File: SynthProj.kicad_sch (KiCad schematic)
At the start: 36 parts, among them J18 Ext In, SW5 SW_DPDT_x2

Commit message: more and more routing
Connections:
- net VCA/Main_Out: now also SW5.3 (C)
- net EchoOut: now reaches SW5.6 (C)
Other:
- note added: "Switch in the echo effect or use the jacks"
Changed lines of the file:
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@@
 (kicad_sch (version 20230121) (generator eeschema)
   (paper "A3")
+  (junction (at 224.155 65.405) (diameter 0) (color 0 0 0 0)
+  )
+  (junction (at 254.635 162.56) (diameter 0) (color 0 0 0 0)
+  )
   (junction (at 181.61 97.155) (diameter 0) (color 0 0 0 0)
   )
   (junction (at 74.93 88.265) (diameter 0) (color 0 0 0 0)
   )
-  (junction (at 224.155 67.945) (diameter 0) (color 0 0 0 0)
-  )
   (junction (at 134.62 162.56) (diameter 0) (color 0 0 0 0)
   )
@@
     (stroke (width 0) (type default))
   )
+  (wire (pts (xy 254.635 108.585) (xy 280.035 108.585))
+    (stroke (width 0) (type default))
+  )
   (wire (pts (xy 72.39 62.865) (xy 81.28 62.865))
     (stroke (width 0) (type default))
@@
     (stroke (width 0) (type default))
   )
-  (wire (pts (xy 351.79 80.01) (xy 363.855 80.01))
+  (wire (pts (xy 217.17 67.945) (xy 243.84 67.945))
+    (stroke (width 0) (type default))
+  )
+  (wire (pts (xy 351.79 80.01) (xy 356.87 80.01))
     (stroke (width 0) (type default))
   )
@@
     (stroke (width 0) (type default))
   )
-  (wire (pts (xy 217.17 67.945) (xy 224.155 67.945))
-    (stroke (width 0) (type default))
-  )
   (wire (pts (xy 175.26 97.155) (xy 181.61 97.155))
     (stroke (width 0) (type default))
@@
     (stroke (width 0) (type default))
   )
-  (wire (pts (xy 217.17 65.405) (xy 229.87 65.405))
+  (wire (pts (xy 217.17 65.405) (xy 224.155 65.405))
     (stroke (width 0) (type default))
   )
@@
     (stroke (width 0) (type default))
   )
+  (wire (pts (xy 254.635 162.56) (xy 266.7 162.56))
+    (stroke (width 0) (type default))
+  )
   (wire (pts (xy 181.61 97.155) (xy 186.69 97.155))
     (stroke (width 0) (type default))
@@
     (stroke (width 0) (type default))
   )
-  (wire (pts (xy 245.11 162.56) (xy 266.7 162.56))
+  (wire (pts (xy 245.11 162.56) (xy 254.635 162.56))
     (stroke (width 0) (type default))
   )
@@
     (stroke (width 0) (type default))
   )
+  (wire (pts (xy 224.155 65.405) (xy 229.87 65.405))
+    (stroke (width 0) (type default))
+  )
   (wire (pts (xy 74.93 57.785) (xy 81.28 57.785))
     (stroke (width 0) (type default))
@@
     (stroke (width 0) (type default))
   )
+  (wire (pts (xy 254.635 162.56) (xy 254.635 108.585))
+    (stroke (width 0) (type default))
+  )
   (wire (pts (xy 132.08 118.745) (xy 132.08 79.375))
     (stroke (width 0) (type default))
@@
     (stroke (width 0) (type default))
   )
+  (wire (pts (xy 133.985 96.52) (xy 144.78 96.52))
+    (stroke (width 0) (type default))
+  )
   (wire (pts (xy 78.74 133.985) (xy 81.28 133.985))
     (stroke (width 0) (type default))
@@
     (stroke (width 0) (type default))
   )
-  (wire (pts (xy 269.24 108.585) (xy 280.035 108.585))
-    (stroke (width 0) (type default))
-  )
   (wire (pts (xy 105.41 116.205) (xy 129.54 116.205))
     (stroke (width 0) (type default))
@@
     (stroke (width 0) (type default))
   )
-  (wire (pts (xy 224.155 67.945) (xy 224.155 92.71))
+  (wire (pts (xy 133.985 84.455) (xy 133.985 96.52))
     (stroke (width 0) (type default))
   )
@@
     (stroke (width 0) (type default))
   )
-  (wire (pts (xy 224.155 67.945) (xy 243.84 67.945))
-    (stroke (width 0) (type default))
-  )
   (wire (pts (xy 241.935 120.65) (xy 235.585 120.65))
     (stroke (width 0) (type default))
@@
     (stroke (width 0) (type default))
   )
+  (wire (pts (xy 224.155 65.405) (xy 224.155 92.71))
+    (stroke (width 0) (type default))
+  )
   (wire (pts (xy 372.745 158.115) (xy 368.935 158.115))
     (stroke (width 0) (type default))
@@
   )
   (wire (pts (xy 338.455 82.55) (xy 341.63 82.55))
+    (stroke (width 0) (type default))
+  )
+  (wire (pts (xy 136.525 84.455) (xy 133.985 84.455))
     (stroke (width 0) (type default))
   )
@@
     (effects (font (size 1.27 1.27)) (justify left bottom))
   )
+  (text "Switch in the echo effect or use the jacks" (at 319.405 71.755 0)
+    (effects (font (size 1.27 1.27)) (justify left bottom))
+  )
   (text "100k 20mm Linear Pot: RK09D1130-F20-C0-B104\n100k 20mm Log Pot: RK09D1130-F20-C0-A104\n\n10k 20mm Linear Pot: RK09D1130-F20-C0-B103\n10k 20mm Log Pot: RK09D1130-F20-C0-V103"
     (at 23.495 234.315 0)
@@
   (text "12 Pole Rotary Switch - Metal MC12L1NCQD 9.4mm shoulder height\n12 Pole Rotary Switch - Plastic RTAP31S12W25FS 12.6mm shoulder height\n12 Pole Rotary Switch - Plastic KC52A10.001NPS 14.2mm shoulder height\n12 Pole Rotary Switch - Plastic SR2612F-0112-21R0B-D8-N 12.6mm shoulder height "
     (at 23.495 263.525 0)
+    (effects (font (size 1.27 1.27)) (justify left bottom))
+  )
+  (label "EchoOut" (at 144.78 96.52 0) (fields_autoplaced)
+    (effects (font (size 1.27 1.27)) (justify left bottom))
+  )
+  (label "EchoOut" (at 356.87 80.01 0) (fields_autoplaced)
     (effects (font (size 1.27 1.27)) (justify left bottom))
   )
@@
     )
   )
+  (global_label "AD1A" (shape input) (at 236.855 67.945 270) (fields_autoplaced)
+    (effects (font (size 1.27 1.27)) (justify right))
+    (property "Intersheetrefs" "${INTERSHEET_REFS}" (at 236.855 74.9327 90)
+      (effects (font (size 1.27 1.27)) (justify right) hide)
+    )
+  )
   (global_label "S&H" (shape input) (at 68.58 123.825 180) (fields_autoplaced)
     (effects (font (size 1.27 1.27)) (justify right))
@@
     )
   )
-  (global_label "AD1A" (shape input) (at 201.295 92.71 90) (fields_autoplaced)
-    (effects (font (size 1.27 1.27)) (justify left))
-    (property "Intersheetrefs" "${INTERSHEET_REFS}" (at 201.295 85.7223 90)
-      (effects (font (size 1.27 1.27)) (justify left) hide)
-    )
-  )
   (global_label "AD1A" (shape input) (at 68.58 65.405 180) (fields_autoplaced)
     (effects (font (size 1.27 1.27)) (justify right))
@@
     )
     (property "Value" "GNDREF" (at 238.76 69.5381 0)
-      (effects (font (size 1.27 1.27)))
+      (effects (font (size 1.27 1.27)) hide)
     )
     (property "Footprint" "" (at 238.76 65.405 0)
@@
     )
     (property "Value" "GNDREF" (at 238.76 82.2381 0)
-      (effects (font (size 1.27 1.27)))
+      (effects (font (size 1.27 1.27)) hide)
     )
     (property "Footprint" "" (at 238.76 78.105 0)
@@
     )
     (property "Value" "GNDREF" (at 195.5292 129.413 0)
-      (effects (font (size 1.27 1.27)))
+      (effects (font (size 1.27 1.27)) hide)
     )
     (property "Footprint" "" (at 191.135 129.54 0)

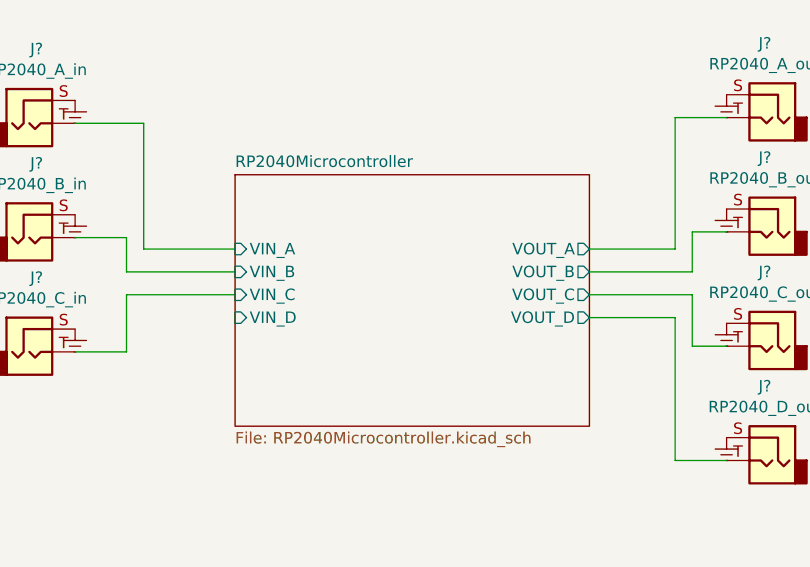
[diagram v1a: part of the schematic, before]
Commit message: routing microcontroller
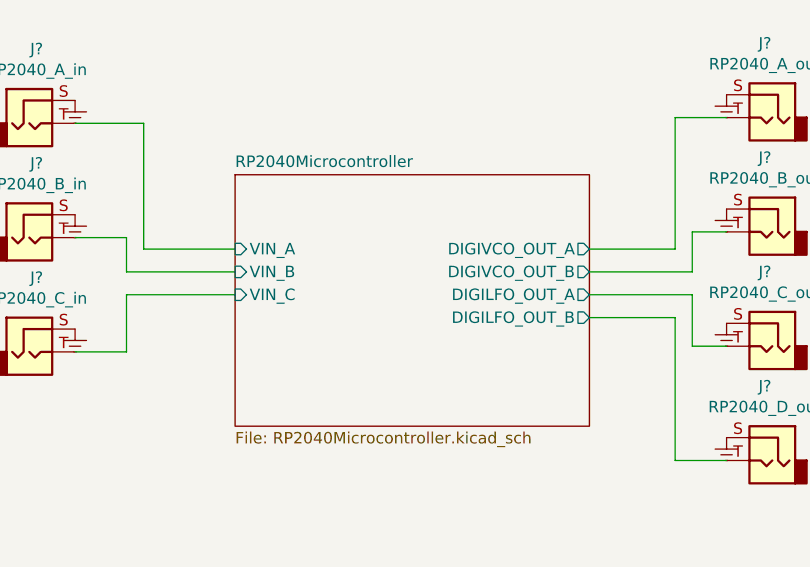
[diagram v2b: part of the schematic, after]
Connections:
- net RP2040Microcontroller/VOUT_A renamed RP2040Microcontroller/DIGIVCO_OUT_A
- net RP2040Microcontroller/VOUT_B renamed RP2040Microcontroller/DIGIVCO_OUT_B
- net RP2040Microcontroller/VOUT_C renamed RP2040Microcontroller/DIGILFO_OUT_A
- net RP2040Microcontroller/VOUT_D renamed RP2040Microcontroller/DIGILFO_OUT_B
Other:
- sheet RP2040Microcontroller ports: added DIGILFO_OUT_A, DIGILFO_OUT_B, DIGIVCO_OUT_A, DIGIVCO_OUT_B; removed VIN_D, VOUT_A, VOUT_B, VOUT_C, VOUT_D
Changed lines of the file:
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@@
       (effects (font (size 1.27 1.27)) (justify left top))
-    )
-    (pin "VIN_D" input (at 318.135 154.94 180)
-      (effects (font (size 1.27 1.27)) (justify left))
     )
     (pin "VIN_C" input (at 318.135 152.4 180)
       (effects (font (size 1.27 1.27)) (justify left))
-    )
-    (pin "VOUT_D" output (at 357.505 154.94 0)
-      (effects (font (size 1.27 1.27)) (justify right))
     )
     (pin "VIN_B" input (at 318.135 149.86 180)
@@
       (effects (font (size 1.27 1.27)) (justify left))
     )
-    (pin "VOUT_B" output (at 357.505 149.86 0)
+    (pin "DIGILFO_OUT_A" output (at 357.505 152.4 0)
       (effects (font (size 1.27 1.27)) (justify right))
     )
-    (pin "VOUT_A" output (at 357.505 147.32 0)
+    (pin "DIGILFO_OUT_B" output (at 357.505 154.94 0)
       (effects (font (size 1.27 1.27)) (justify right))
     )
-    (pin "VOUT_C" output (at 357.505 152.4 0)
+    (pin "DIGIVCO_OUT_A" output (at 357.505 147.32 0)
       (effects (font (size 1.27 1.27)) (justify right))
     )
+    (pin "DIGIVCO_OUT_B" output (at 357.505 149.86 0)
+      (effects (font (size 1.27 1.27)) (justify right))
+    )

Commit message: more and more and more and more and more routing
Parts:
- removed J?: RP2040_C_in, SynthProjConnectors:PJ-301-BM, symbol SynthProj-rescue:AudioJack2-Connector
- added J?: Mixer Ext InC, SynthProjConnectors:PJ-301-BM, symbol SynthProj-rescue:AudioJack2-Connector
- added J?: Mixer Ext InB, SynthProjConnectors:PJ-301-BM, symbol SynthProj-rescue:AudioJack2-Connector
- added SW9: SW_SPDT, SynthProjConnectors:SMTS-102, symbol Switch:SW_SPDT
- J?: value RP2040_A_out -> RP2040_VCO_A
- J?: value RP2040_B_out -> RP2040_VCO_B
- J?: value Mixer Ext In -> Mixer Ext InA
- J?: value RP2040_C_out -> RP2040_LFO_A
- J?: value RP2040_D_out -> RP2040_LFO_B
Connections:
- net GNDREF: now also J?.S, J?.S
- net RP2040Microcontroller/VIN_A: now also SW9.2 (B); no longer J?.T
- net VCA/Main_Out: now also SW9.1 (A)
- net Mixer/Mixer_ExtIn renamed Mixer/Mixer_ExtIn1
- new net: J?.T, SW9.3 (C)
- new net Mixer/Mixer_ExtIn2: J?.T
- new net Mixer/Mixer_ExtIn3: J?.T
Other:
- sheet Mixer ports: added Mixer_ExtIn1, Mixer_ExtIn2, Mixer_ExtIn3; removed Mixer_ExtIn
- sheet RP2040Microcontroller ports: added none; removed VIN_C
- note added: "Patch audio out into microcontroller"
- note added: "Switch in the echo effect, or use the jacks"
- note removed: "Switch in the echo effect or use the jacks"
- moved on the sheet: J?

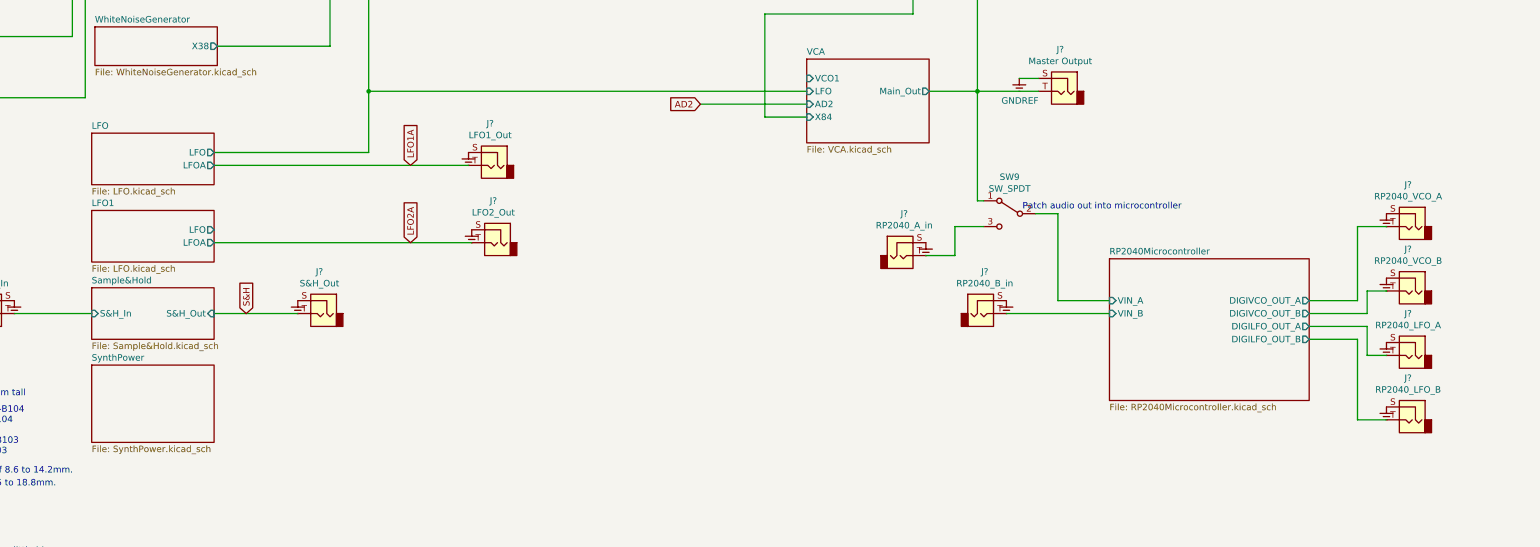
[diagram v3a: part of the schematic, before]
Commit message: Removed microcontroller and power stuff to simplify
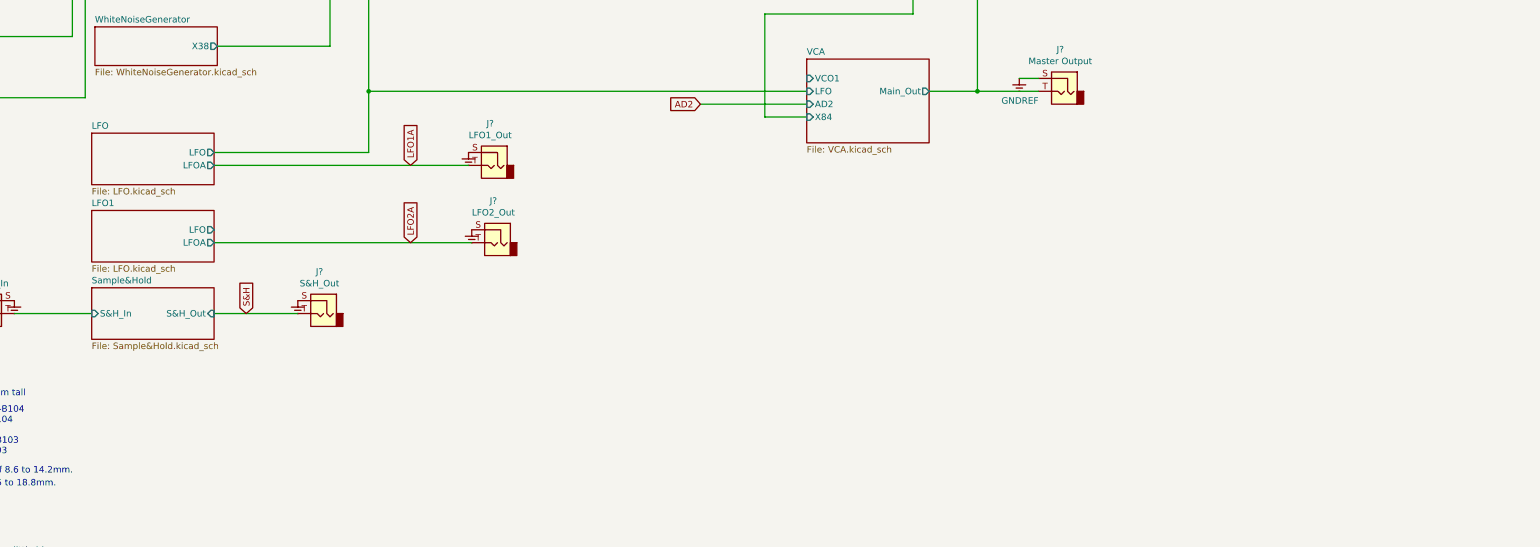
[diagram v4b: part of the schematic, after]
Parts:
- removed J?: RP2040_VCO_A, SynthProjConnectors:PJ-301-BM, symbol SynthProj-rescue:AudioJack2-Connector
- removed J?: RP2040_VCO_B, SynthProjConnectors:PJ-301-BM, symbol SynthProj-rescue:AudioJack2-Connector
- removed J?: RP2040_A_in, SynthProjConnectors:PJ-301-BM, symbol SynthProj-rescue:AudioJack2-Connector
- removed J?: RP2040_LFO_A, SynthProjConnectors:PJ-301-BM, symbol SynthProj-rescue:AudioJack2-Connector
- removed J?: RP2040_LFO_B, SynthProjConnectors:PJ-301-BM, symbol SynthProj-rescue:AudioJack2-Connector
- removed J?: RP2040_B_in, SynthProjConnectors:PJ-301-BM, symbol SynthProj-rescue:AudioJack2-Connector
- removed SW9: SW_SPDT, SynthProjConnectors:SMTS-102, symbol Switch:SW_SPDT
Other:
- removed sheet RP2040Microcontroller
- removed sheet SynthPower
- note removed: "Patch audio out into microcontroller"

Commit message: finished routing!
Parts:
- added C? (x2): 470nF, Capacitor_SMD:C_0805_2012Metric, symbol Device:C
- added C? (x2): 4.7uF, Capacitor_SMD:C_0805_2012Metric, symbol Device:C
- added C? (x2): 47nF, Capacitor_SMD:C_0603_1608Metric, symbol Device:C
- added J29: Conn_01x16_Pin, Connector_PinHeader_2.54mm:PinHeader_2x08_P2.54mm_Vertical, symbol Connector:Conn_01x16_Pin
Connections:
- net GNDREF: now also C?.1, C?.1, C?.1, C?.2, C?.2, C?.2, J29.3 (Pin_3), J29.4 (Pin_4), J29.5 (Pin_5), J29.6 (Pin_6), J29.7 (Pin_7), J29.8 (Pin_8)
- new net: J29.11 (Pin_11), J29.12 (Pin_12)
- new net: J29.13 (Pin_13), J29.14 (Pin_14)
- new net: J29.15 (Pin_15), J29.16 (Pin_16)
- new net +12V: C?.2, C?.2, C?.2, J29.10 (Pin_10), J29.9 (Pin_9)
- new net -12V: C?.1, C?.1, C?.1, J29.1 (Pin_1), J29.2 (Pin_2)
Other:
- note added: "+5V"
- note added: "CV"
- note added: "EuroRack Power Header"
- note added: "Gate"
